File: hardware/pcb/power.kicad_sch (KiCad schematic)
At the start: 58 parts, among them IC1 MCP16502AB, U3 TPS7A2033PDBV, U4 BQ25640, U5 MAX17260

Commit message: small stuff
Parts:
- added TP66: -BAT, TestPoint:TestPoint_Pad_D1.0mm, symbol Connector:TestPoint
- added TP67: +BAT, TestPoint:TestPoint_Pad_D1.0mm, symbol Connector:TestPoint
- BT1: footprint (none) -> Connector_JST:JST_GH_SM02B-GHS-TB_1x02-1MP_P1.25mm_Horizontal
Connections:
- net +BATT: now also TP67.1
- net GND: now also BT1.MP
- net at BT1.2 (-), R29.1, U5.9 (CSPL): now also TP66.1

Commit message: smol
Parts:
- BT1: LCSC (none) -> C189893; MPN (none) -> SM02B-GHS-TB(LF)(SN)
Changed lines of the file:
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@@
 			)
 		)
-		(property "KLC_S3.3" ""
+		(property "MPN" "SM02B-GHS-TB(LF)(SN)"
 			(at 135.89 175.26 0)
 			(hide yes)
@@
 			)
 		)
-		(property "KLC_S4.1" ""
+		(property "LCSC" "C189893"
 			(at 135.89 175.26 0)
 			(hide yes)

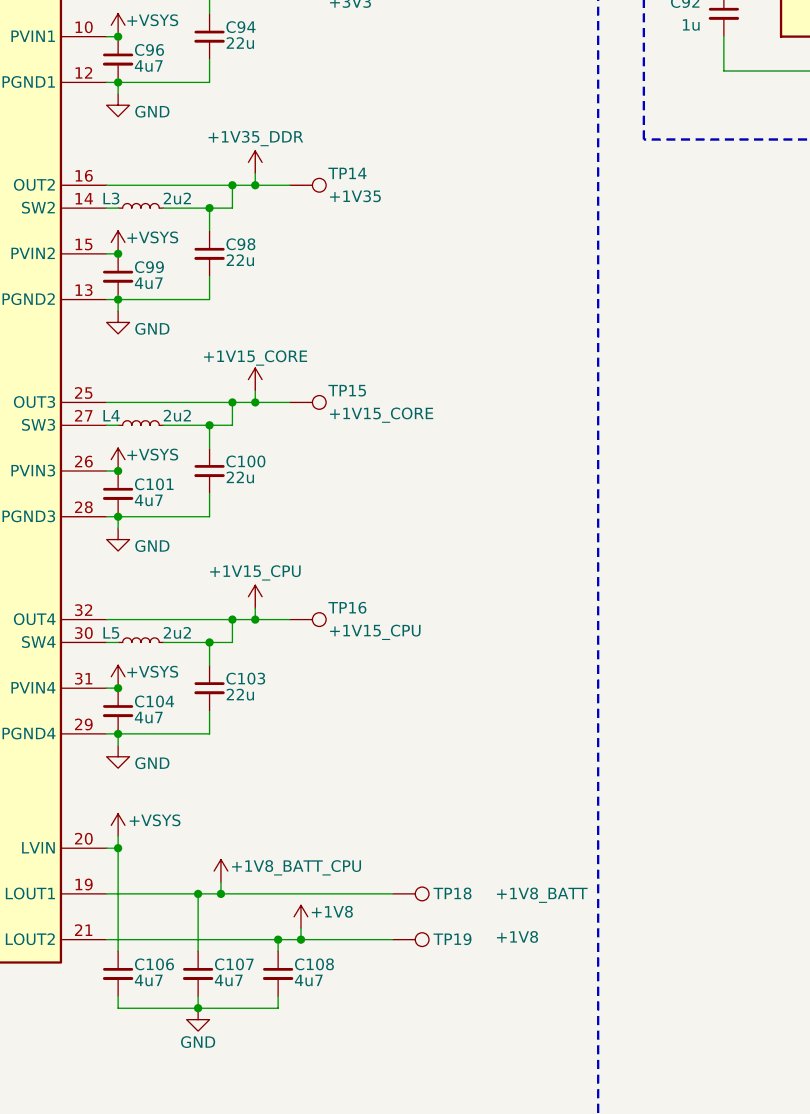
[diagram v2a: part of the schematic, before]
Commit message: laid out caps for vdd ddr, added custom rule area for bgas
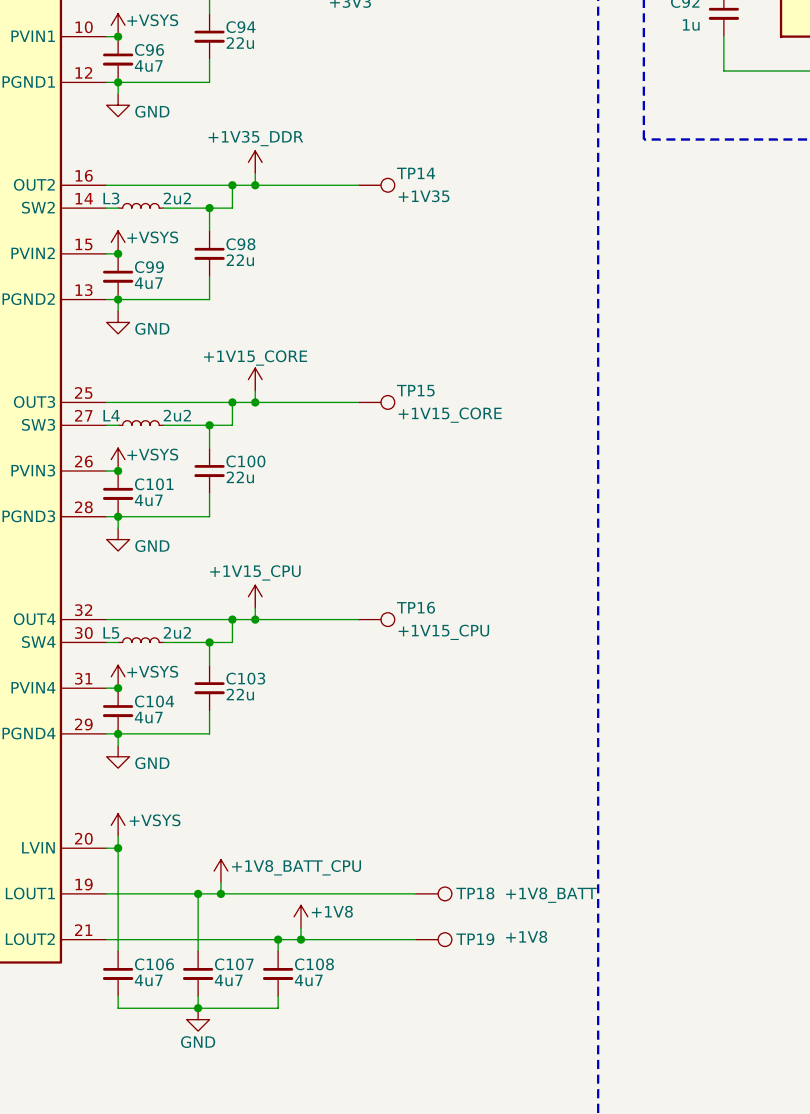
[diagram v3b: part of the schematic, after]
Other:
- moved on the sheet: TP14, TP15, TP16, TP18, TP19

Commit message: layout and power routing
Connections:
- net SW: now reaches C95.2, L2.1, U4.4 (SW)
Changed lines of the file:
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@@
+		)
+	)
+	(label "SW"
+		(at 134.62 93.98 0)
+		(effects
+			(font
+				(size 1.27 1.27)
+			)
+			(justify left bottom)
 		)
 	)

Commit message: pwr
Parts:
- removed TP66: -BAT, TestPoint:TestPoint_Pad_D1.0mm, symbol Connector:TestPoint
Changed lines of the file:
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@@
-	(symbol
-		(lib_id "Connector:TestPoint")
-		(at 135.89 180.34 270)
-		(mirror x)
-		(unit 1)
-		(body_style 1)
-		(exclude_from_sim no)
-		(in_bom yes)
-		(on_board yes)
-		(in_pos_files yes)
-		(dnp no)
-		(property "Reference" "TP66"
-			(at 140.462 180.34 90)
-			(show_name no)
-			(do_not_autoplace no)
-			(effects
-				(font
-					(size 1.27 1.27)
-				)
-				(justify left)
-			)
-		)
-		(property "Value" "-BAT"
-			(at 145.542 180.34 90)
-			(show_name no)
-			(do_not_autoplace no)
-			(effects
-				(font
-					(size 1.27 1.27)
-				)
-				(justify left)
-			)
-		)
-		(property "Footprint" "TestPoint:TestPoint_Pad_D1.0mm"
-			(at 135.89 175.26 0)
-			(hide yes)
-			(show_name no)
-			(do_not_autoplace no)
-			(effects
-				(font
-					(size 1.27 1.27)
-				)
-			)
-		)
-		(property "Datasheet" ""
-			(at 135.89 175.26 0)
-			(hide yes)
-			(show_name no)
-			(do_not_autoplace no)
-			(effects
-				(font
-					(size 1.27 1.27)
-				)
-			)
-		)
-		(property "Description" "test point"
-			(at 135.89 180.34 0)
-			(hide yes)
-			(show_name no)
-			(do_not_autoplace no)
-			(effects
-				(font
-					(size 1.27 1.27)
-				)
-			)
-		)
-		(pin "1"
-		)
-		(instances
-			(project "meko"
-				(path "/da54f10a-146b-4941-a9c7-55c7173bb101/608c30f2-ff67-48b2-81d8-ecb6ade86a50"
-					(reference "TP66")
-					(unit 1)
-				)
-			)
-		)
-	)
 	(symbol
 		(lib_id "Connector:TestPoint")

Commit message: cleanup, tespoints, passives
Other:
- moved on the sheet: TP12
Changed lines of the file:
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@@
 	(wire
 		(pts
-			(xy 358.14 87.63) (xy 370.84 87.63)
+			(xy 358.14 87.63) (xy 373.38 87.63)
 		)
 		(stroke
@@
 		)
 	)
+	(netclass_flag ""
+		(length 2.54)
+		(shape round)
+		(at 370.84 87.63 0)
+		(fields_autoplaced yes)
+		(effects
+			(font
+				(size 1.27 1.27)
+			)
+			(justify left bottom)
+		)
+		(property "Netclass" "PWR"
+			(at 371.5385 85.09 0)
+			(show_name no)
+			(do_not_autoplace no)
+			(effects
+				(font
+					(size 1.27 1.27)
+				)
+				(justify left)
+			)
+		)
+		(property "Component Class" ""
+			(at -5.08 -29.21 0)
+			(show_name no)
+			(do_not_autoplace no)
+			(effects
+				(font
+					(size 1.27 1.27)
+					(italic yes)
+				)
+			)
+		)
+	)
 	(symbol
 		(lib_id "power:+BATT")
@@
 	(symbol
 		(lib_id "Connector:TestPoint")
-		(at 370.84 87.63 270)
+		(at 373.38 87.63 270)
 		(mirror x)
 		(unit 1)
@@
 		(dnp no)
 		(property "Reference" "TP12"
-			(at 375.158 86.36 90)
+			(at 377.698 86.36 90)
 			(show_name no)
 			(do_not_autoplace no)
@@
 		)
 		(property "Value" "+3V3"
-			(at 375.158 88.9 90)
+			(at 377.698 88.9 90)
 			(show_name no)
 			(do_not_autoplace no)
@@
 		)
 		(property "Footprint" "TestPoint:TestPoint_Pad_D1.0mm"
-			(at 370.84 82.55 0)
+			(at 373.38 82.55 0)
 			(hide yes)
 			(show_name no)
@@
 		)
 		(property "Datasheet" ""
-			(at 370.84 82.55 0)
+			(at 373.38 82.55 0)
 			(hide yes)
 			(show_name no)
@@
 		)
 		(property "Description" "test point"
-			(at 370.84 87.63 0)
+			(at 373.38 87.63 0)
 			(hide yes)
 			(show_name no)

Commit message: more cleanup, more testpoints, more passives
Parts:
- removed TP18: +1V8_BATT, TestPoint:TestPoint_Pad_D1.0mm, symbol Connector:TestPoint
- added TP7: GND, TestPoint:TestPoint_Pad_D1.0mm, symbol Connector:TestPoint
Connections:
- net GND: now also TP7.1
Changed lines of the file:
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@@
 	)
 	(junction
+		(at 276.86 190.5)
+		(diameter 0)
+		(color 0 0 0 0)
+	)
+	(junction
 		(at 267.97 124.46)
 		(diameter 0)
@@
 	)
 	(junction
+		(at 279.4 190.5)
+		(diameter 0)
+		(color 0 0 0 0)
+	)
+	(junction
 		(at 195.58 110.49)
 		(diameter 0)
@@
 	)
 	(junction
-		(at 279.4 190.5)
-		(diameter 0)
-		(color 0 0 0 0)
-	)
-	(junction
 		(at 278.13 162.56)
 		(diameter 0)
@@
 	)
 	(junction
-		(at 276.86 190.5)
-		(diameter 0)
-		(color 0 0 0 0)
-	)
-	(junction
 		(at 85.09 110.49)
 		(diameter 0)
@@
 	(wire
 		(pts
-			(xy 276.86 190.5) (xy 300.99 190.5)
-		)
-		(stroke
-			(width 0)
-			(type default)
-		)
-	)
-	(wire
-		(pts
 			(xy 358.14 86.36) (xy 358.14 87.63)
 		)
@@
 	(wire
 		(pts
+			(xy 276.86 190.5) (xy 279.4 190.5)
+		)
+		(stroke
+			(width 0)
+			(type default)
+		)
+	)
+	(wire
+		(pts
 			(xy 187.96 133.35) (xy 200.66 133.35)
 		)
@@
 	(wire
 		(pts
+			(xy 279.4 190.5) (xy 298.45 190.5)
+		)
+		(stroke
+			(width 0)
+			(type default)
+		)
+	)
+	(wire
+		(pts
 			(xy 187.96 105.41) (xy 208.28 105.41)
 		)
@@
 	(wire
 		(pts
+			(xy 193.04 232.41) (xy 193.04 233.68)
+		)
+		(stroke
+			(width 0)
+			(type default)
+		)
+	)
+	(wire
+		(pts
 			(xy 187.96 130.81) (xy 210.82 130.81)
 		)
@@
 	)
 	(symbol
+		(lib_id "power:GND")
+		(at 193.04 233.68 0)
+		(unit 1)
+		(body_style 1)
+		(exclude_from_sim no)
+		(in_bom yes)
+		(on_board yes)
+		(in_pos_files yes)
+		(dnp no)
+		(property "Reference" "#PWR0147"
+			(at 193.04 240.03 0)
+			(hide yes)
+			(show_name no)
+			(do_not_autoplace no)
+			(effects
+				(font
+					(size 1.27 1.27)
+				)
+			)
+		)
+		(property "Value" "GND"
+			(at 196.85 235.712 0)
+			(show_name no)
+			(do_not_autoplace no)
+			(effects
+				(font
+					(size 1.27 1.27)
+				)
+			)
+		)
+		(property "Footprint" ""
+			(at 193.04 233.68 0)
+			(hide yes)
+			(show_name no)
+			(do_not_autoplace no)
+			(effects
+				(font
+					(size 1.27 1.27)
+				)
+			)
+		)
+		(property "Datasheet" ""
+			(at 193.04 233.68 0)
+			(hide yes)
+			(show_name no)
+			(do_not_autoplace no)
+			(effects
+				(font
+					(size 1.27 1.27)
+				)
+			)
+		)
+		(property "Description" "Power symbol creates a global label with name \"GND\" , ground"
+			(at 193.04 233.68 0)
+			(hide yes)
+			(show_name no)
+			(do_not_autoplace no)
+			(effects
+				(font
+					(size 1.27 1.27)
+				)
+			)
+		)
+		(pin "1"
+		)
+		(instances
+			(project "meko"
+				(path "/da54f10a-146b-4941-a9c7-55c7173bb101/608c30f2-ff67-48b2-81d8-ecb6ade86a50"
+					(reference "#PWR0147")
+					(unit 1)
+				)
+			)
+		)
+	)
+	(symbol
 		(lib_id "Connector:TestPoint")
 		(at 294.64 111.76 270)
@@
 	)
 	(symbol
-		(lib_id "Connector:TestPoint")
-		(at 300.99 190.5 270)
-		(mirror x)
-		(unit 1)
-		(body_style 1)
-		(exclude_from_sim no)
-		(in_bom yes)
-		(on_board yes)
-		(in_pos_files yes)
-		(dnp no)
-		(property "Reference" "TP18"
-			(at 305.562 190.5 90)
-			(show_name no)
-			(do_not_autoplace no)
-			(effects
-				(font
-					(size 1.27 1.27)
-				)
-				(justify left)
-			)
-		)
-		(property "Value" "+1V8_BATT"
-			(at 310.896 190.5 90)
-			(show_name no)
-			(do_not_autoplace no)
-			(effects
-				(font
-					(size 1.27 1.27)
-				)
-				(justify left)
-			)
-		)
-		(property "Footprint" "TestPoint:TestPoint_Pad_D1.0mm"
-			(at 300.99 185.42 0)
-			(hide yes)
-			(show_name no)
-			(do_not_autoplace no)
-			(effects
-				(font
-					(size 1.27 1.27)
-				)
-			)
-		)
-		(property "Datasheet" ""
-			(at 300.99 185.42 0)
-			(hide yes)
-			(show_name no)
-			(do_not_autoplace no)
-			(effects
-				(font
-					(size 1.27 1.27)
-				)
-			)
-		)
-		(property "Description" "test point"
-			(at 300.99 190.5 0)
-			(hide yes)
-			(show_name no)
-			(do_not_autoplace no)
-			(effects
-				(font
-					(size 1.27 1.27)
-				)
-			)
-		)
-		(pin "1"
-		)
-		(instances
-			(project "meko"
-				(path "/da54f10a-146b-4941-a9c7-55c7173bb101/608c30f2-ff67-48b2-81d8-ecb6ade86a50"
-					(reference "TP18")
-					(unit 1)
-				)
-			)
-		)
-	)
-	(symbol
 		(lib_id "Device:C_Small")
 		(at 355.6 92.71 0)
@@
 					(unit 1)
 				)
+			)
+		)
+	)
+	(symbol
+		(lib_id "Connector:TestPoint")
+		(at 193.04 232.41 0)
+		(mirror y)
+		(unit 1)
+		(body_style 1)
+		(exclude_from_sim no)
+		(in_bom yes)
+		(on_board yes)
+		(in_pos_files yes)
+		(dnp no)
+		(property "Reference" "TP7"
+			(at 193.04 224.282 0)
+			(show_name no)
+			(do_not_autoplace no)
+			(effects
+				(font
+					(size 1.27 1.27)
+				)
+			)
+		)
+		(property "Value" "GND"
+			(at 193.04 226.822 0)
+			(show_name no)
+			(do_not_autoplace no)
+			(effects
+				(font
+					(size 1.27 1.27)
+				)
+			)
+		)
+		(property "Footprint" "TestPoint:TestPoint_Pad_D1.0mm"
+			(at 187.96 232.41 0)
+			(hide yes)
+			(show_name no)
+			(do_not_autoplace no)
+			(effects
+				(font
+					(size 1.27 1.27)
+				)
+			)
+		)
+		(property "Datasheet" ""
+			(at 187.96 232.41 0)
+			(hide yes)
+			(show_name no)
+			(do_not_autoplace no)
+			(effects
+				(font
+					(size 1.27 1.27)
+				)
+			)
+		)
+		(property "Description" "test point"
+			(at 193.04 232.41 0)
+			(hide yes)
+			(show_name no)
+			(do_not_autoplace no)
+			(effects
+				(font
+					(size 1.27 1.27)
+				)
+			)
+		)
+		(pin "1"
+		)
+		(instances
+			(project "meko"
+				(path "/da54f10a-146b-4941-a9c7-55c7173bb101/608c30f2-ff67-48b2-81d8-ecb6ade86a50"
+					(reference "TP7")
+					(unit 1)
+				)

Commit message: updated edge cut
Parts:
- R20: footprint Resistor_SMD:R_0402_1005Metric -> Resistor_SMD:R_0201_0603Metric
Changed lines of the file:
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@@
 			)
 		)
-		(property "Footprint" "Resistor_SMD:R_0402_1005Metric"
+		(property "Footprint" "Resistor_SMD:R_0201_0603Metric"
 			(at 195.58 101.6 0)
 			(hide yes)
